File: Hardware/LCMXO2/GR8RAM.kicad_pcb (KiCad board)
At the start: 4 copper layers, 99.9 x 59.8 mm, 101 parts, among them J1 AppleIIBus, J2 microUSB, J3 Flash, J4 JTAG, SW1 FW, U1 LCMXO2-640HC-4TG100C, U10 AP2127K-1.2TRG1, U11 74AHCT1G125GW, U12 74AHCT245PW, U13 25M, U14 74AHCT1G125GW, U2 W9825G6KH-6, U3 W25Q128JVSIQ, U4 74LVC245APW, U5 74LVC245APW, U6 74AHC245PW, U7 CH340G, U8 XC6206P332MR, U9 74LVC245APW, Y1 12M

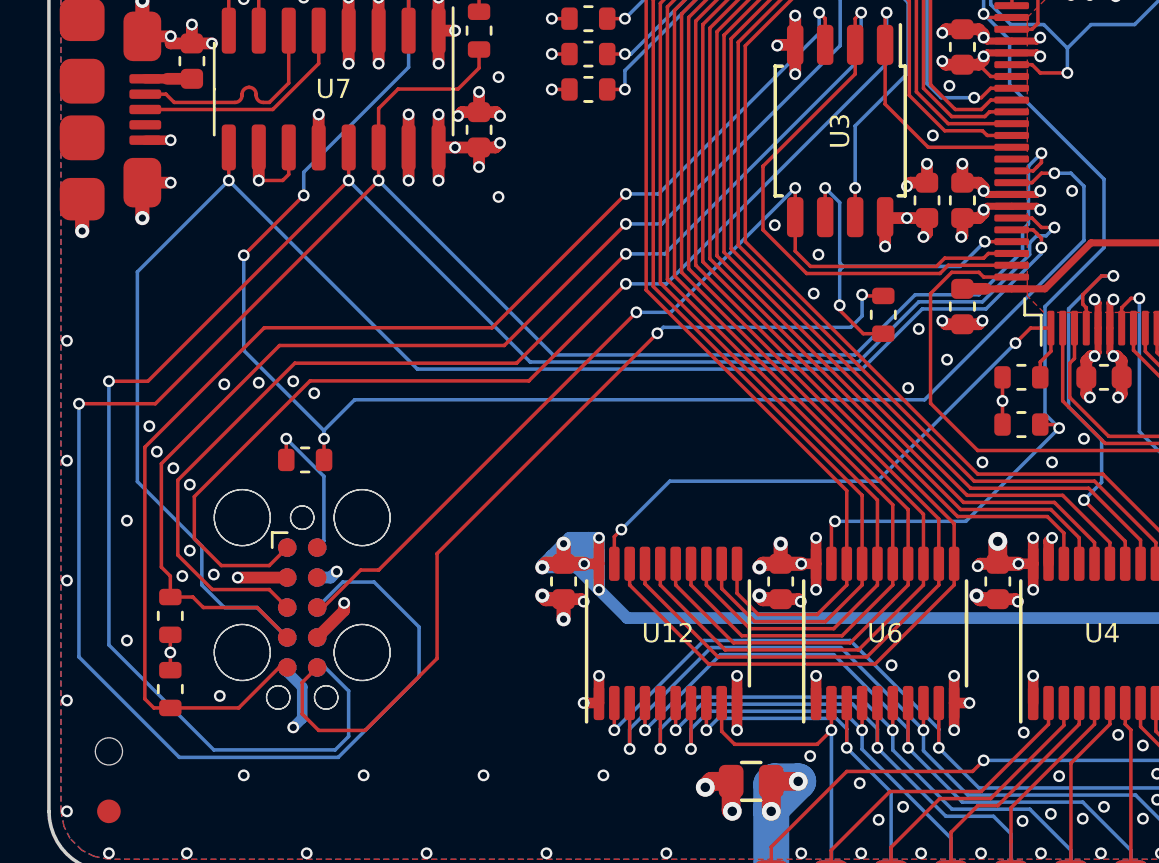
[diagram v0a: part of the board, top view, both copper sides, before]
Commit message: Update Tag-Connect TC2050 footprint
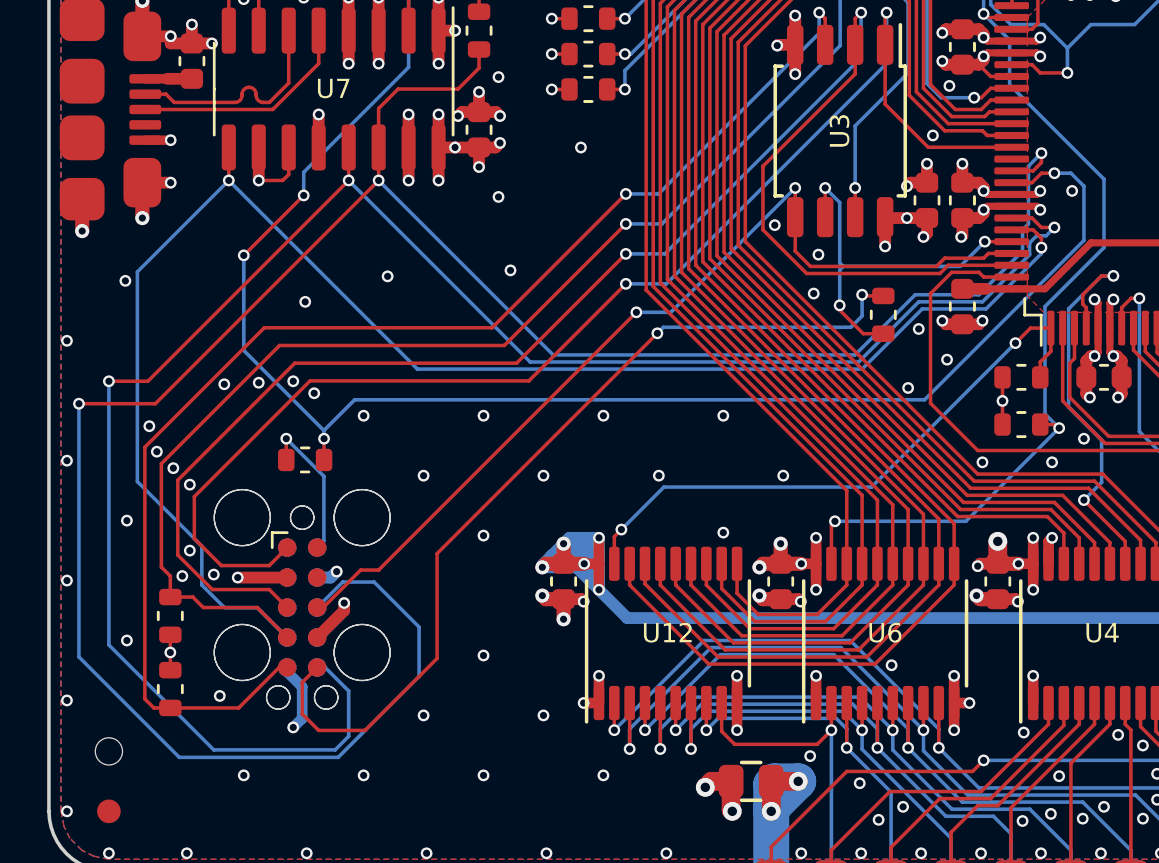
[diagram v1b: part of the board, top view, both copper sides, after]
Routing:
- net GND: vias 419 -> 437
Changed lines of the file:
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@@
     (property "ki_keywords" "connector")
     (attr exclude_from_pos_files)
-    (fp_text reference "J3" (at -0.9525 0 -90) (layer "F.Fab")
+    (fp_text reference "J3" (at -0.9525 0 90) (layer "F.Fab")
         (effects (font (size 0.8128 0.8128) (thickness 0.2032) bold))
     )
-    (fp_text value "Flash" (at -0.9525 1.27 -90) (layer "F.Fab")
+    (fp_text value "Flash" (at -0.9525 1.27 90) (layer "F.Fab")
         (effects (font (size 0.8128 0.8128) (thickness 0.2032) bold))
     )
-    (fp_text user "KEEPOUT" (at 0 0 -90) (layer "Cmts.User")
+    (fp_text user "KEEPOUT" (at 0 0 90) (layer "Cmts.User")
         (effects (font (size 0.4 0.4) (thickness 0.07)))
     )
@@
       (polygon
         (pts
-          (xy 55.6895 118.364)
-          (xy 55.6895 123.444)
-          (xy 56.9595 123.444)
-          (xy 56.9595 118.364)
+          (xy 55.5625 118.237)
+          (xy 55.5625 123.571)
+          (xy 57.0865 123.571)
+          (xy 57.0865 118.237)
         )
       )
@@
       (polygon
         (pts
-          (xy 56.9595 118.364)
-          (xy 56.9595 123.444)
-          (xy 55.6895 123.444)
-          (xy 55.6895 118.364)
+          (xy 57.0865 118.237)
+          (xy 57.0865 123.571)
+          (xy 55.5625 123.571)
+          (xy 55.5625 118.237)
         )
       )
@@
   (via (at 76.35 104.7) (size 0.5) (drill 0.3) (layers "F.Cu" "B.Cu") (net 2))
   (via (at 118.11 131.318) (size 0.5) (drill 0.3) (layers "F.Cu" "B.Cu") (net 2))
+  (via (at 64.008 122.936) (size 0.5) (drill 0.3) (layers "F.Cu" "B.Cu") (net 2))
   (via (at 98.4 110.25) (size 0.5) (drill 0.3) (layers "F.Cu" "B.Cu") (net 2))
   (via (at 127.45 104.3) (size 0.6) (drill 0.3) (layers "F.Cu" "B.Cu") (net 2))
@@
   (via (at 97.663 80.645) (size 0.5) (drill 0.3) (layers "F.Cu" "B.Cu") (net 2))
   (via (at 138.303 116.205) (size 0.5) (drill 0.3) (layers "F.Cu" "B.Cu") (net 2))
+  (via (at 61.468 115.316) (size 0.5) (drill 0.3) (layers "F.Cu" "B.Cu") (net 2))
   (via (at 104.95 102.6) (size 0.5) (drill 0.3) (layers "F.Cu" "B.Cu") (net 2))
   (via (at 72.263 80.645) (size 0.5) (drill 0.3) (layers "F.Cu" "B.Cu") (net 2))
@@
   (via (at 87.6 96.75) (size 0.5) (drill 0.3) (layers "F.Cu" "B.Cu") (net 2))
   (via (at 138.303 80.645) (size 0.5) (drill 0.3) (layers "F.Cu" "B.Cu") (net 2))
+  (via (at 76.708 115.316) (size 0.5) (drill 0.3) (layers "F.Cu" "B.Cu") (net 2))
   (via (at 77.343 85.725) (size 0.5) (drill 0.3) (layers "F.Cu" "B.Cu") (net 2))
   (via (at 115.443 88.265) (size 0.5) (drill 0.3) (layers "F.Cu" "B.Cu") (net 2))
@@
   (via (at 144.78 123.825) (size 0.5) (drill 0.3) (layers "F.Cu" "B.Cu") (net 2))
   (via (at 109.1 113.7) (size 0.5) (drill 0.3) (layers "F.Cu" "B.Cu") (net 2))
+  (via (at 65.151 106.6165) (size 0.5) (drill 0.3) (layers "F.Cu" "B.Cu") (net 2))
   (via (at 85.2 96.75) (size 0.5) (drill 0.3) (layers "F.Cu" "B.Cu") (net 2))
   (via (at 77.85 127.2) (size 0.5) (drill 0.3) (layers "F.Cu" "B.Cu") (net 2))
@@
   (via (at 143.383 90.805) (size 0.5) (drill 0.3) (layers "F.Cu" "B.Cu") (net 2))
   (via (at 130.35 122.4) (size 0.5) (drill 0.3) (layers "F.Cu" "B.Cu") (net 2))
+  (via (at 66.548 125.476) (size 0.5) (drill 0.3) (layers "F.Cu" "B.Cu") (net 2))
   (via (at 102.85 98.4) (size 0.5) (drill 0.3) (layers "F.Cu" "B.Cu") (net 2))
   (via (at 64.7065 100.076) (size 0.5) (drill 0.3) (layers "F.Cu" "B.Cu") (net 2))
   (via (at 114.05 111.85) (size 0.5) (drill 0.3) (layers "F.Cu" "B.Cu") (net 2))
   (via (at 90.9 112) (size 0.5) (drill 0.3) (layers "F.Cu" "B.Cu") (net 2))
+  (via (at 48.8315 107.061) (size 0.5) (drill 0.3) (layers "F.Cu" "B.Cu") (net 2))
   (via (at 97.45 126.9) (size 0.5) (drill 0.3) (layers "F.Cu" "B.Cu") (net 2))
   (via (at 95 127.9) (size 0.5) (drill 0.3) (layers "F.Cu" "B.Cu") (net 2))
@@
   (via (at 50.673 94.615) (size 0.5) (drill 0.3) (layers "F.Cu" "B.Cu") (net 2))
   (via (at 110.8 102.45) (size 0.6) (drill 0.3) (layers "F.Cu" "B.Cu") (net 2))
+  (via (at 64.008 117.856) (size 0.5) (drill 0.3) (layers "F.Cu" "B.Cu") (net 2))
   (via (at 128.27 131.318) (size 0.5) (drill 0.3) (layers "F.Cu" "B.Cu") (net 2))
   (via (at 102.743 85.725) (size 0.5) (drill 0.3) (layers "F.Cu" "B.Cu") (net 2))
@@
   (via (at 69.723 83.185) (size 0.5) (drill 0.3) (layers "F.Cu" "B.Cu") (net 2))
   (via (at 112.05 115.35) (size 0.5) (drill 0.3) (layers "F.Cu" "B.Cu") (net 2))
+  (via (at 74.168 112.776) (size 0.5) (drill 0.3) (layers "F.Cu" "B.Cu") (net 2))
   (via (at 77.343 80.645) (size 0.5) (drill 0.3) (layers "F.Cu" "B.Cu") (net 2))
   (via (at 93.15 126.1) (size 0.5) (drill 0.3) (layers "F.Cu" "B.Cu") (net 2))
@@
   (via (at 58.1025 120.7135) (size 0.5) (drill 0.3) (layers "F.Cu" "B.Cu") (net 2))
   (via (at 59.944 84.328) (size 0.5) (drill 0.3) (layers "F.Cu" "B.Cu") (net 2))
+  (via (at 68.1355 101.4095) (size 0.5) (drill 0.3) (layers "F.Cu" "B.Cu") (net 2))
   (via (at 144.78 82.423) (size 0.5) (drill 0.3) (layers "F.Cu" "B.Cu") (net 2))
   (via (at 133.223 85.725) (size 0.5) (drill 0.3) (layers "F.Cu" "B.Cu") (net 2))
@@
   (via (at 61.595 131.318) (size 0.5) (drill 0.3) (layers "F.Cu" "B.Cu") (net 2))
   (via (at 81.95 103.05) (size 0.5) (drill 0.3) (layers "F.Cu" "B.Cu") (net 2))
+  (via (at 59.944 106.8705) (size 0.5) (drill 0.3) (layers "F.Cu" "B.Cu") (net 2))
   (via (at 50.75 101.1) (size 0.5) (drill 0.3) (layers "F.Cu" "B.Cu") (net 2))
+  (via (at 69.088 112.776) (size 0.5) (drill 0.3) (layers "F.Cu" "B.Cu") (net 2))
   (via (at 143.383 95.885) (size 0.5) (drill 0.3) (layers "F.Cu" "B.Cu") (net 2))
   (via (at 125.55 104.65) (size 0.5) (drill 0.3) (layers "F.Cu" "B.Cu") (net 2))
@@
   (via (at 134 118.95) (size 0.8) (drill 0.4) (layers "F.Cu" "B.Cu") (net 2))
   (via (at 133.223 111.125) (size 0.5) (drill 0.3) (layers "F.Cu" "B.Cu") (net 2))
+  (via (at 61.468 125.476) (size 0.5) (drill 0.3) (layers "F.Cu" "B.Cu") (net 2))
   (via (at 111.75 103.05) (size 0.5) (drill 0.3) (layers "F.Cu" "B.Cu") (net 2))
   (via (at 117.983 80.645) (size 0.5) (drill 0.3) (layers "F.Cu" "B.Cu") (net 2))
@@
   (via (at 94.1 120.4) (size 0.6) (drill 0.3) (layers "F.Cu" "B.Cu") (net 2))
   (via (at 95.123 88.265) (size 0.5) (drill 0.3) (layers "F.Cu" "B.Cu") (net 2))
+  (via (at 58.928 112.776) (size 0.5) (drill 0.3) (layers "F.Cu" "B.Cu") (net 2))
   (via (at 52.324 94.5515) (size 0.5) (drill 0.3) (layers "F.Cu" "B.Cu") (net 2))
   (via (at 62.103 90.805) (size 0.5) (drill 0.3) (layers "F.Cu" "B.Cu") (net 2))
@@
   (via (at 102.35 126.1) (size 0.5) (drill 0.3) (layers "F.Cu" "B.Cu") (net 2))
   (via (at 46.355 114.681) (size 0.5) (drill 0.3) (layers "F.Cu" "B.Cu") (net 2))
+  (via (at 71.4375 115.316) (size 0.5) (drill 0.3) (layers "F.Cu" "B.Cu") (net 2))
   (via (at 125.6 94.15) (size 0.5) (drill 0.3) (layers "F.Cu" "B.Cu") (net 2))
   (via (at 60.833 100.0125) (size 0.5) (drill 0.3) (layers "F.Cu" "B.Cu") (net 2))
@@
   (via (at 92.55 127.95) (size 0.5) (drill 0.3) (layers "F.Cu" "B.Cu") (net 2))
   (via (at 125.603 83.185) (size 0.5) (drill 0.3) (layers "F.Cu" "B.Cu") (net 2))
+  (via (at 74.168 117.729) (size 0.5) (drill 0.3) (layers "F.Cu" "B.Cu") (net 2))
   (via (at 113.1 120.5) (size 0.5) (drill 0.3) (layers "F.Cu" "B.Cu") (net 2))
+  (via (at 66.548 115.316) (size 0.5) (drill 0.3) (layers "F.Cu" "B.Cu") (net 2))
   (via (at 114.05 113.45) (size 0.5) (drill 0.3) (layers "F.Cu" "B.Cu") (net 2))
   (via (at 63.8175 99.06) (size 0.5) (drill 0.3) (layers "F.Cu" "B.Cu") (net 2))
@@
   (via (at 48.895 122.301) (size 0.5) (drill 0.3) (layers "F.Cu" "B.Cu") (net 2))
   (via (at 126.45 105.4) (size 0.6) (drill 0.3) (layers "F.Cu" "B.Cu") (net 2))
+  (via (at 56.4515 107.95) (size 0.5) (drill 0.3) (layers "F.Cu" "B.Cu") (net 2))
   (via (at 102.743 80.645) (size 0.5) (drill 0.3) (layers "F.Cu" "B.Cu") (net 2))
   (via (at 130.35 117.65) (size 0.8) (drill 0.4) (layers "F.Cu" "B.Cu") (net 2))
@@
   (via (at 128.143 85.725) (size 0.5) (drill 0.3) (layers "F.Cu" "B.Cu") (net 2))
   (via (at 46.355 93.472) (size 0.5) (drill 0.3) (layers "F.Cu" "B.Cu") (net 2))
+  (via (at 64.008 112.776) (size 0.5) (drill 0.3) (layers "F.Cu" "B.Cu") (net 2))
   (via (at 55.9435 111.3155) (size 0.5) (drill 0.3) (layers "F.Cu" "B.Cu") (net 2))
   (via (at 50.165 114.3) (size 0.5) (drill 0.3) (layers "F.Cu" "B.Cu") (net 2))
@@
   (via (at 86.55 109.7) (size 0.5) (drill 0.3) (layers "F.Cu" "B.Cu") (net 154))
   (via (at 69.85 117.6) (size 0.5) (drill 0.3) (layers "F.Cu" "B.Cu") (net 154))
-  (segment (start 80.7 115.55) (end 71.9 115.55) (width 0.15) (layer "B.Cu") (net 154))
-  (segment (start 71.9 115.55) (end 69.85 117.6) (width 0.15) (layer "B.Cu") (net 154))
-  (segment (start 86.55 109.7) (end 80.7 115.55) (width 0.15) (layer "B.Cu") (net 154))
+  (segment (start 71.65 115.8) (end 69.85 117.6) (width 0.15) (layer "B.Cu") (net 154))
+  (segment (start 80.45 115.8) (end 71.65 115.8) (width 0.15) (layer "B.Cu") (net 154))
+  (segment (start 86.55 109.7) (end 80.45 115.8) (width 0.15) (layer "B.Cu") (net 154))
   (segment (start 69.25 98.95) (end 70 98.95) (width 0.15) (layer "F.Cu") (net 155))
   (segment (start 86.3875 95.9) (end 85.35 95.9) (width 0.15) (layer "F.Cu") (net 155))

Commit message: dip switch stuff
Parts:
- added R24: 47, stdpads:R_0603, F.Cu at (94.9, 91.7)
- added R25: 10k, stdpads:R_0603, F.Cu at (103.4, 91.5)
- added R26: 10k, stdpads:R_0603, F.Cu at (104.9, 91.5)
- added R27: 10k, stdpads:R_0603, F.Cu at (101.9, 91.5)
- SW1: footprint stdpads:SW_DIP_SPSTx02_Slide_DSHP02TS_P1.27mm -> stdpads:SW_DIP_SPSTx03_Slide_DSHP03TS_P1.27mm
- moved SW1 5.08 mm to (135.8, 90.8)
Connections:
- SW1 pad 3: /FW0 -> GND
- SW1 pad 4: /FW1 -> /FW0
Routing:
- net /~{RESTORE}: track 0.00 -> 44.8 mm, vias 0 -> 2
- net +3V3: track 169.5 -> 176.7 mm
- net /FW0: track 50.8 -> 55.0 mm, vias 2 -> 3
- net /FW1: track 48.4 -> 52.4 mm, vias 2 -> 3
- net /RD0: track 63.7 -> 66.4 mm
- net GND: track 218.2 -> 219.6 mm, vias 437 -> 424
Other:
- board text added: "16"
- board text added: "Disable Restore"
- board text added: "Enable Restore"
- board text added: "MB RAMFactor*"
- board text added: "Restore Partition:"

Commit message: Another board RC
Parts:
- R24: value 47 -> 2k2
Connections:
- net /ACLK renamed /CLKin
- net /IRQ~{OE} renamed /~{IRQ}out
- net /RA13 renamed /BA13
- net /RA14 renamed /BA14
- net /RA15 renamed /BA15
- net /RES~{OE} renamed /~{RES}out
- net /RPHI0 renamed /BPHI0
- net /RR~{W}in renamed /BR~{W}
- net /R~{DEVSEL} renamed /B~{DEVSEL}
- net /R~{IOSEL} renamed /B~{IOSEL}
- net /R~{IOSTRB} renamed /B~{IOSTRB}
- net /R~{RES} renamed /B~{RES}
- net /SBA0 renamed /RBA0
- net /SBA1 renamed /RBA1
- net /SCKE renamed /RCKE
- net /SDQMH renamed /DQMH
- net /SDQML renamed /DQML
- net /S~{CAS} renamed /~{CAS}
- net /S~{CS} renamed /R~{CS}
- net /S~{RAS} renamed /~{RAS}
- net /S~{WE} renamed /R~{WE}
- R2 pad 1: /RCLK -> /RCLKr
- R2 pad 2: /RCLKout -> /RCLK
- R24 pad 2: /RD0 -> /BD0
- U1 pad 2: /RA9 -> /BA9
- U1 pad 21: /SD2 -> /RD2
- U1 pad 24: /SD1 -> /RD1
- U1 pad 25: /SD0 -> /RD0
- U1 pad 27: /SD3 -> /RD3
- U1 pad 28: /SD4 -> /RD4
- U1 pad 29: /SD5 -> /RD5
- U1 pad 3: /RA10 -> /BA10
- U1 pad 30: /SD6 -> /RD6
- U1 pad 31: /SD7 -> /RD7
- U1 pad 39: /RCLKout -> /RCLK
- U1 pad 4: /RA4 -> /BA4
- U1 pad 42: /SA12 -> /RA12
- U1 pad 45: /SA11 -> /RA11
- U1 pad 47: /SA10 -> /RA10
- U1 pad 49: /SA9 -> /RA9
- U1 pad 51: /SA4 -> /RA4
- U1 pad 52: /SA5 -> /RA5
- U1 pad 53: /SA8 -> /RA8
- U1 pad 54: /SA0 -> /RA0
- U1 pad 57: /SA7 -> /RA7
- U1 pad 58: /SA2 -> /RA2
- U1 pad 59: /SA1 -> /RA1
- U1 pad 60: /SA3 -> /RA3
- U1 pad 61: (no net) -> unconnected-(U1-NC-Pad61)
- U1 pad 62: /SA6 -> /RA6
- U1 pad 65: /RD0 -> /BD0
- U1 pad 66: /RD1 -> /BD1
- U1 pad 67: /RD2 -> /BD2
- U1 pad 68: /RD3 -> /BD3
- U1 pad 69: /RD4 -> /BD4
- U1 pad 70: /RD5 -> /BD5
- U1 pad 71: /RD6 -> /BD6
- U1 pad 74: /RA0 -> /BA0
- U1 pad 75: /RD7 -> /BD7
- U1 pad 78: /RA1 -> /BA1
- U1 pad 8: /RA11 -> /BA11
- U1 pad 83: /RA2 -> /BA2
- U1 pad 84: /RA3 -> /BA3
- U1 pad 85: /RA5 -> /BA5
- U1 pad 86: /RA6 -> /BA6
- U1 pad 87: /RA7 -> /BA7
- U1 pad 9: /RA12 -> /BA12
- U1 pad 99: /RA8 -> /BA8
- U12 pad 11: /RD0 -> /BD0
- U12 pad 12: /RD1 -> /BD1
- U12 pad 13: /RD2 -> /BD2
- U12 pad 14: /RD3 -> /BD3
- U12 pad 15: /RD4 -> /BD4
- U12 pad 16: /RD5 -> /BD5
- U12 pad 17: /RD6 -> /BD6
- U12 pad 18: /RD7 -> /BD7
- U2 pad 10: /SD5 -> /RD5
- U2 pad 11: /SD6 -> /RD6
- U2 pad 13: /SD7 -> /RD7
- U2 pad 2: /SD0 -> /RD0
- U2 pad 22: /SA10 -> /RA10
- U2 pad 23: /SA0 -> /RA0
- U2 pad 24: /SA1 -> /RA1
- U2 pad 25: /SA2 -> /RA2
- U2 pad 26: /SA3 -> /RA3
- U2 pad 29: /SA4 -> /RA4
- U2 pad 30: /SA5 -> /RA5
- U2 pad 31: /SA6 -> /RA6
- U2 pad 32: /SA7 -> /RA7
- U2 pad 33: /SA8 -> /RA8
- U2 pad 34: /SA9 -> /RA9
- U2 pad 35: /SA11 -> /RA11
- U2 pad 36: /SA12 -> /RA12
- U2 pad 38: /RCLK -> /RCLKr
- U2 pad 4: /SD1 -> /RD1
- U2 pad 42: /SD7 -> /RD7
- U2 pad 44: /SD6 -> /RD6
- U2 pad 45: /SD5 -> /RD5
- U2 pad 47: /SD4 -> /RD4
- U2 pad 48: /SD3 -> /RD3
- U2 pad 5: /SD2 -> /RD2
- U2 pad 50: /SD2 -> /RD2
- U2 pad 51: /SD1 -> /RD1
- U2 pad 53: /SD0 -> /RD0
- U2 pad 7: /SD3 -> /RD3
- U2 pad 8: /SD4 -> /RD4
- U4 pad 11: /RA7 -> /BA7
- U4 pad 12: /RA6 -> /BA6
- U4 pad 13: /RA5 -> /BA5
- U4 pad 14: /RA4 -> /BA4
- U4 pad 15: /RA3 -> /BA3
- U4 pad 16: /RA2 -> /BA2
- U4 pad 17: /RA1 -> /BA1
- U4 pad 18: /RA0 -> /BA0
- U6 pad 11: /RD7 -> /BD7
- U6 pad 12: /RD6 -> /BD6
- U6 pad 13: /RD5 -> /BD5
- U6 pad 14: /RD4 -> /BD4
- U6 pad 15: /RD3 -> /BD3
- U6 pad 16: /RD2 -> /BD2
- U6 pad 17: /RD1 -> /BD1
- U6 pad 18: /RD0 -> /BD0
- U9 pad 14: /RA12 -> /BA12
- U9 pad 15: /RA11 -> /BA11
- U9 pad 16: /RA10 -> /BA10
- U9 pad 17: /RA9 -> /BA9
- U9 pad 18: /RA8 -> /BA8
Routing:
- net /BD6: track 0.00 -> 68.9 mm, vias 0 -> 2
- net /BD5: track 0.00 -> 66.7 mm
- net /BD0: track 0.00 -> 66.4 mm
- net /BD4: track 0.00 -> 66.0 mm
- net /BD3: track 0.00 -> 65.2 mm
- net /BD2: track 0.00 -> 64.7 mm
- net /BD1: track 0.00 -> 64.2 mm
- net /BD7: track 0.00 -> 63.0 mm
- net /BA2: track 0.00 -> 50.7 mm, vias 0 -> 2
- net /BA5: track 0.00 -> 50.4 mm
- net /BA3: track 0.00 -> 50.1 mm
- net /BA6: track 0.00 -> 50.1 mm
- net /BA0: track 0.00 -> 50.1 mm
- net /BA7: track 0.00 -> 49.9 mm
- net /BA1: track 0.00 -> 49.8 mm
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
